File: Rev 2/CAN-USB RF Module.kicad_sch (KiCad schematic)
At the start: 32 parts, among them IC1 ESDALC6V1W5, J1 Conn_02x05_Top_Bottom, J5 Conn_Coaxial, SW1 RESET, SW2 BOOT0, U1 8MHz, U2 STM32L442KCU6

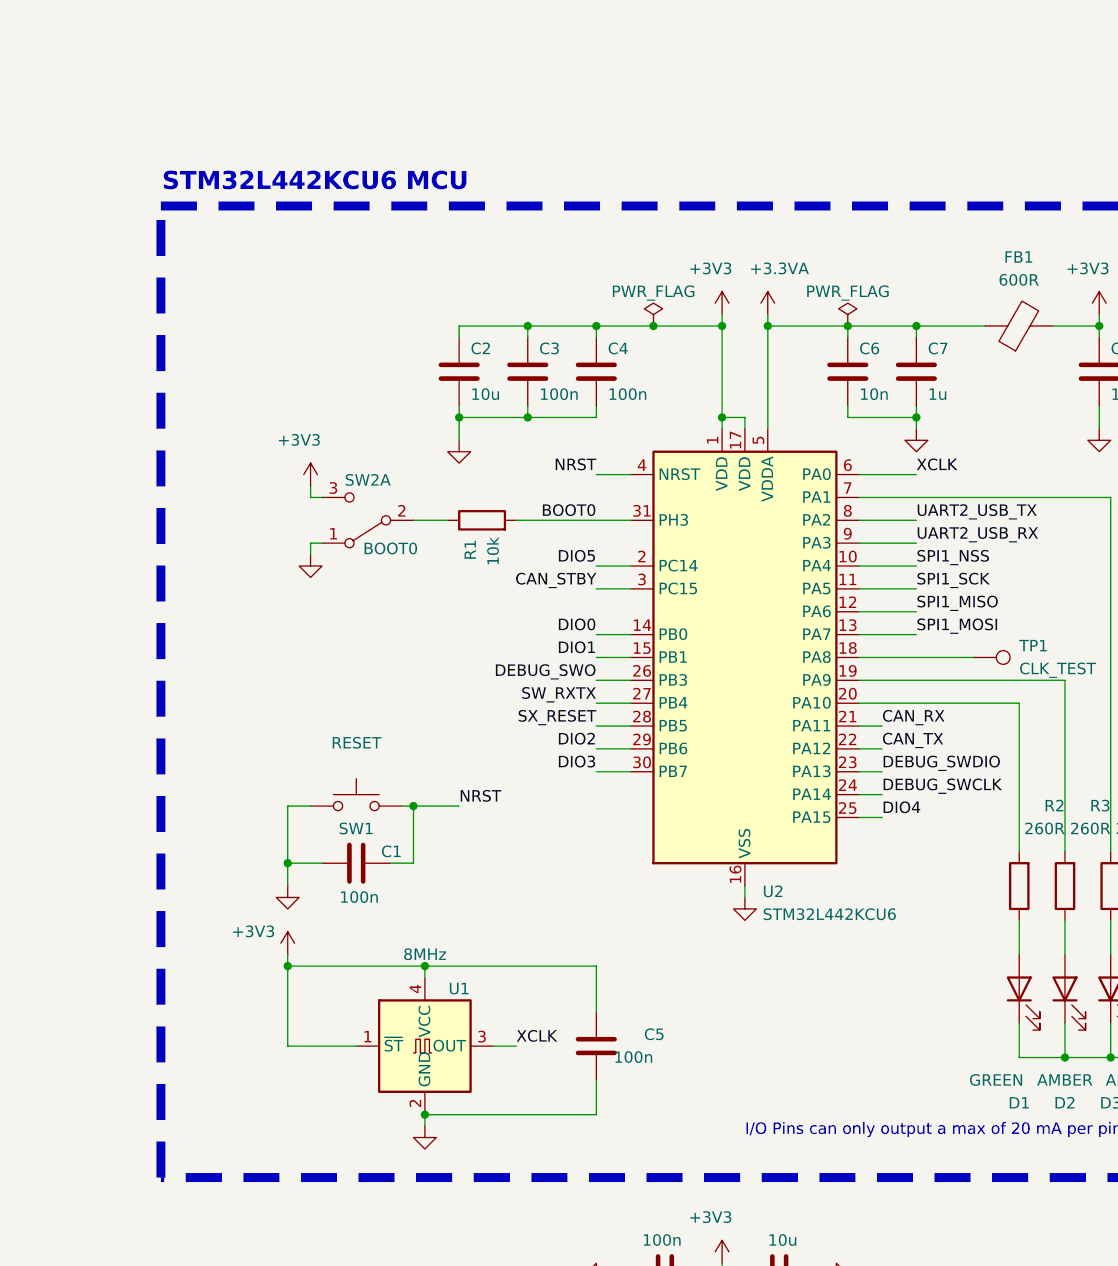
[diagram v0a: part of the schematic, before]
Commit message: added GPSW and HW DB
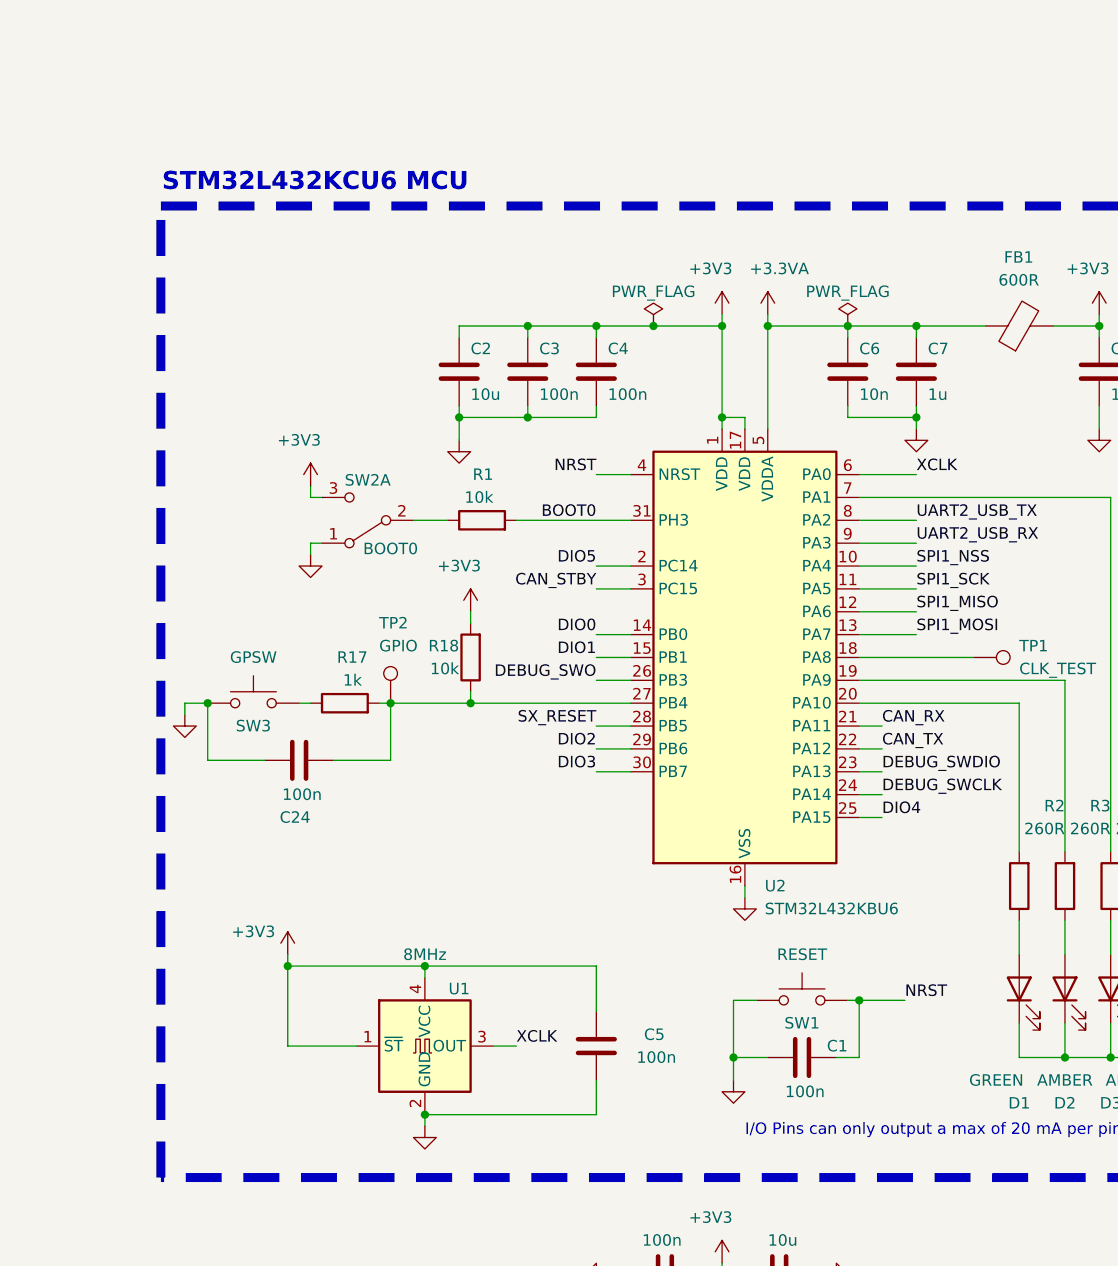
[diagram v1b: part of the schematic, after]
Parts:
- removed U2: STM32L442KCU6, Package_DFN_QFN:QFN-32-1EP_5x5mm_P0.5mm_EP3.45x3.45mm, symbol MCU_ST_STM32L4:STM32L442KCUx
- added C24: 100n, Capacitor_SMD:C_0402_1005Metric, symbol Device:C
- added R17: 1k, Resistor_SMD:R_0805_2012Metric, symbol Device:R
- added R18: 10k, Resistor_SMD:R_0603_1608Metric, symbol Device:R
- added SW3: GPSW, Button_Switch_SMD:SW_SPST_PTS810, symbol Switch:SW_Push
- added TP2: GPIO, TestPoint:TestPoint_Pad_1.0x1.0mm, symbol Connector:TestPoint
- added U2: STM32L432KBU6, Package_DFN_QFN:QFN-32-1EP_5x5mm_P0.5mm_EP3.45x3.45mm, symbol MCU_ST_STM32L4:STM32L432KBUx
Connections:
- net +3.3VA: now also U2.5 (VDDA)
- net +3V3: now also R18.2, U2.1 (VDD), U2.17 (VDD)
- net BOOT0: now also U2.31 (PH3)
- net CAN_RX: now also U2.21 (PA11)
- net CAN_STBY: now also U2.3 (PC15)
- net CAN_TX: now also U2.22 (PA12)
- net DEBUG_SWCLK: now also U2.24 (PA14)
- net DEBUG_SWDIO: now also U2.23 (PA13)
- net DEBUG_SWO: now also U2.26 (PB3)
- net DIO0: now also U2.14 (PB0)
- net DIO1: now also U2.15 (PB1)
- net DIO2: now also U2.29 (PB6)
- net DIO3: now also U2.30 (PB7)
- net DIO4: now also U2.25 (PA15)
- net DIO5: now also U2.2 (PC14)
- net GND: now also C24.1, SW3.1, U2.16 (VSS), U2.32 (VSS), U2.33 (VSS)
- net NRST: now also U2.4 (NRST)
- net SPI1_MISO: now also U2.12 (PA6)
- net SPI1_MOSI: now also U2.13 (PA7)
- net SPI1_NSS: now also U2.10 (PA4)
- net SPI1_SCK: now also U2.11 (PA5)
- net SX_RESET: now also U2.28 (PB5)
- net UART2_USB_RX: now also U2.9 (PA3)
- net UART2_USB_TX: now also U2.8 (PA2)
- net XCLK: now also U2.6 (PA0)
- net at R3.2: now also U2.19 (PA9)
- net at R4.2: now also U2.7 (PA1)
- net at R2.2: now also U2.20 (PA10)
- net at TP1.1: now also U2.18 (PA8)
- new net: C24.2, R17.2, R18.1, TP2.1, U2.27 (PB4)
- new net: R17.1, SW3.2
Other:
- note added: "STM32L432KCU6 MCU"
- note removed: "STM32L442KCU6 MCU"
- moved on the sheet: C1, SW1

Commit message: added GPSW and HW DB
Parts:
- D4: JLCPCB Part#(optional) C283619 -> (none); LCSC # C283619 -> (none)
- IC1: JLCPCB Part#(optional) C2827626 -> (none); LCSC # C2827626 -> (none)
- J1: JLCPCB Part#(optional) C5116482 -> (none); LCSC # C5116482 -> (none)
- R18: footprint Resistor_SMD:R_0603_1608Metric -> Resistor_SMD:R_0805_2012Metric
- SW1, SW3: JLCPCB Part#(optional) C221896 -> (none); LCSC # C221896 -> (none)
- SW2: JLCPCB Part#(optional) C221841 -> (none); LCSC # C221841 -> (none)
- U1: JLCPCB Part#(optional) C558766 -> (none); LCSC # C558766 -> (none)
- U2: JLCPCB Part#(optional) (none) -> C94784; LCSC # (none) -> C94784
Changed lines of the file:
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@@
       (effects (font (size 1.27 1.27)) hide)
     )
-    (property "LCSC #" "C5116482" (at 306.07 74.93 0)
-      (effects (font (size 1.27 1.27)) hide)
-    )
-    (property "JLCPCB Part#(optional)" "C5116482" (at 306.07 74.93 0)
+    (property "LCSC #" "" (at 306.07 74.93 0)
+      (effects (font (size 1.27 1.27)) hide)
+    )
+    (property "JLCPCB Part#(optional)" "" (at 306.07 74.93 0)
       (effects (font (size 1.27 1.27)) hide)
     )
@@
       (effects (font (size 1.27 1.27)) hide)
     )
-    (property "LCSC #" "C283619" (at 274.32 71.12 0)
-      (effects (font (size 1.27 1.27)) hide)
-    )
-    (property "JLCPCB Part#(optional)" "C283619" (at 274.32 71.12 0)
+    (property "LCSC #" "" (at 274.32 71.12 0)
+      (effects (font (size 1.27 1.27)) hide)
+    )
+    (property "JLCPCB Part#(optional)" "" (at 274.32 71.12 0)
       (effects (font (size 1.27 1.27)) hide)
     )
@@
       (effects (font (size 1.27 1.27)) (justify left))
     )
-    (property "Footprint" "Resistor_SMD:R_0603_1608Metric" (at 145.288 81.28 90)
+    (property "Footprint" "Resistor_SMD:R_0805_2012Metric" (at 145.288 81.28 90)
       (effects (font (size 1.27 1.27)) hide)
     )
@@
       (effects (font (size 1.27 1.27)) hide)
     )
-    (property "LCSC #" "C2827626" (at 294.64 53.34 0)
-      (effects (font (size 1.27 1.27)) hide)
-    )
-    (property "JLCPCB Part#(optional)" "C2827626" (at 294.64 53.34 0)
+    (property "LCSC #" "" (at 294.64 53.34 0)
+      (effects (font (size 1.27 1.27)) hide)
+    )
+    (property "JLCPCB Part#(optional)" "" (at 294.64 53.34 0)
       (effects (font (size 1.27 1.27)) hide)
     )
@@
       (effects (font (size 1.27 1.27)) hide)
     )
-    (property "LCSC #" "C221896" (at 119.38 86.36 0)
-      (effects (font (size 1.27 1.27)) hide)
-    )
-    (property "JLCPCB Part#(optional)" "C221896" (at 119.38 86.36 0)
+    (property "LCSC #" "" (at 119.38 86.36 0)
+      (effects (font (size 1.27 1.27)) hide)
+    )
+    (property "JLCPCB Part#(optional)" "" (at 119.38 86.36 0)
       (effects (font (size 1.27 1.27)) hide)
     )
@@
       (effects (font (size 1.27 1.27)) hide)
     )
-    (property "LCSC #" "C558766" (at 138.43 124.46 0)
-      (effects (font (size 1.27 1.27)) hide)
-    )
-    (property "JLCPCB Part#(optional)" "C558766" (at 138.43 124.46 0)
+    (property "LCSC #" "" (at 138.43 124.46 0)
+      (effects (font (size 1.27 1.27)) hide)
+    )
+    (property "JLCPCB Part#(optional)" "" (at 138.43 124.46 0)
       (effects (font (size 1.27 1.27)) hide)
     )
@@
       (effects (font (size 1.27 1.27)) hide)
     )
-    (property "LCSC #" "C221841" (at 132.08 66.04 0)
-      (effects (font (size 1.27 1.27)) hide)
-    )
-    (property "JLCPCB Part#(optional)" "C221841" (at 132.08 66.04 0)
+    (property "LCSC #" "" (at 132.08 66.04 0)
+      (effects (font (size 1.27 1.27)) hide)
+    )
+    (property "JLCPCB Part#(optional)" "" (at 132.08 66.04 0)
       (effects (font (size 1.27 1.27)) hide)
     )
@@
       (effects (font (size 1.27 1.27)) hide)
     )
-    (property "LCSC #" "C221896" (at 180.34 119.38 0)
-      (effects (font (size 1.27 1.27)) hide)
-    )
-    (property "JLCPCB Part#(optional)" "C221896" (at 180.34 119.38 0)
+    (property "LCSC #" "" (at 180.34 119.38 0)
+      (effects (font (size 1.27 1.27)) hide)
+    )
+    (property "JLCPCB Part#(optional)" "" (at 180.34 119.38 0)
       (effects (font (size 1.27 1.27)) hide)
     )
@@
       (effects (font (size 1.27 1.27)) hide)
     )
+    (property "JLCPCB Part#(optional)" "C94784" (at 173.99 81.28 0)
+      (effects (font (size 1.27 1.27)) hide)
+    )
+    (property "LCSC #" "C94784" (at 173.99 81.28 0)
+      (effects (font (size 1.27 1.27)) hide)
+    )

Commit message: Thats it no more changes
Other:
- moved on the sheet: C22, C23, J5, MOD1

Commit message: S
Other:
- note added: "STM32L432KBU6 MCU"
- note added: "Use KCU6 instead"
- note removed: "STM32L432KCU6 MCU"
- moved on the sheet: H1, H2, H3, H4
